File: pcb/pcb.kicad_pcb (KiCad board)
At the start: 2 copper layers, 190.5 x 85.7 mm, 98 parts, among them J1 OLED, SW1 RotaryEncoder_Switch, U1 Elite-C

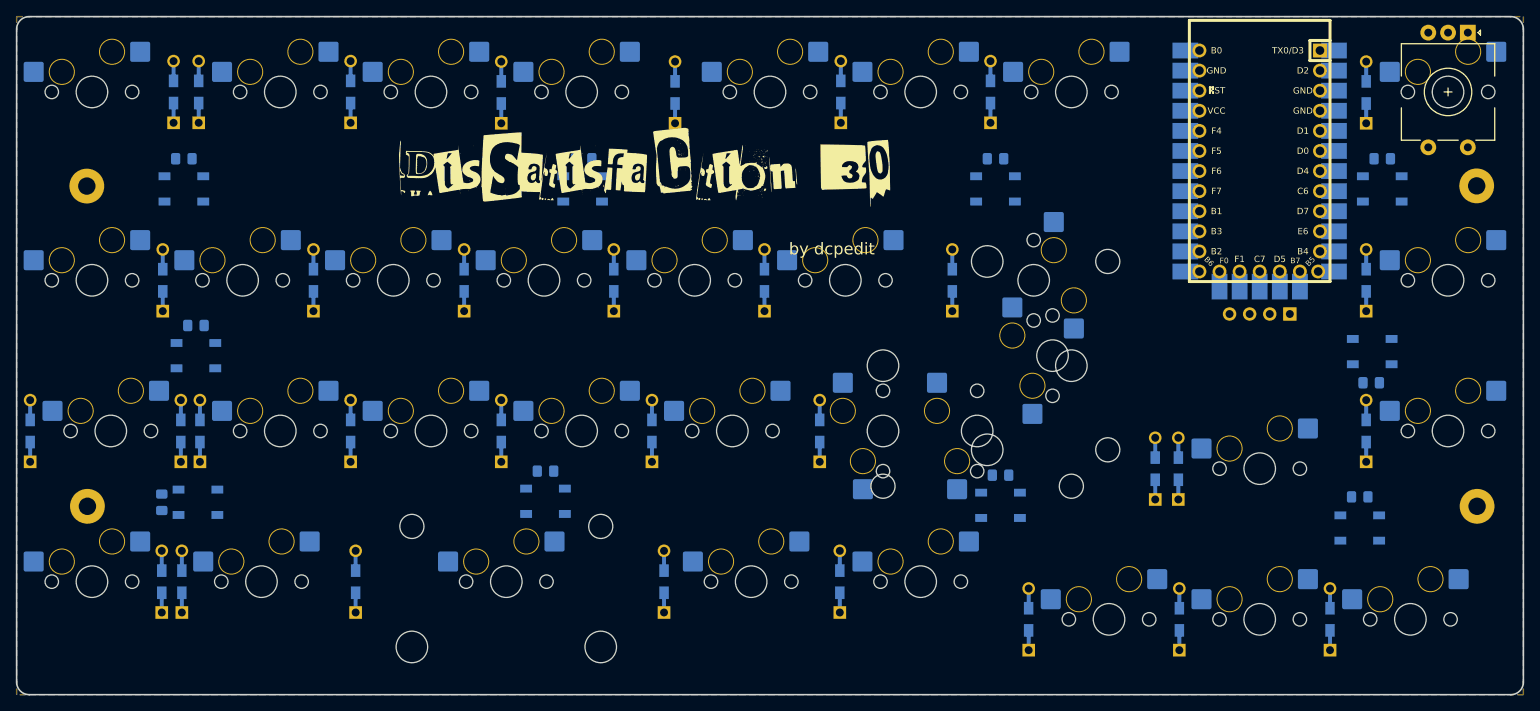
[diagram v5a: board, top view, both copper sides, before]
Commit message: Routed power and switch matrix. Pending connections to the MCU.
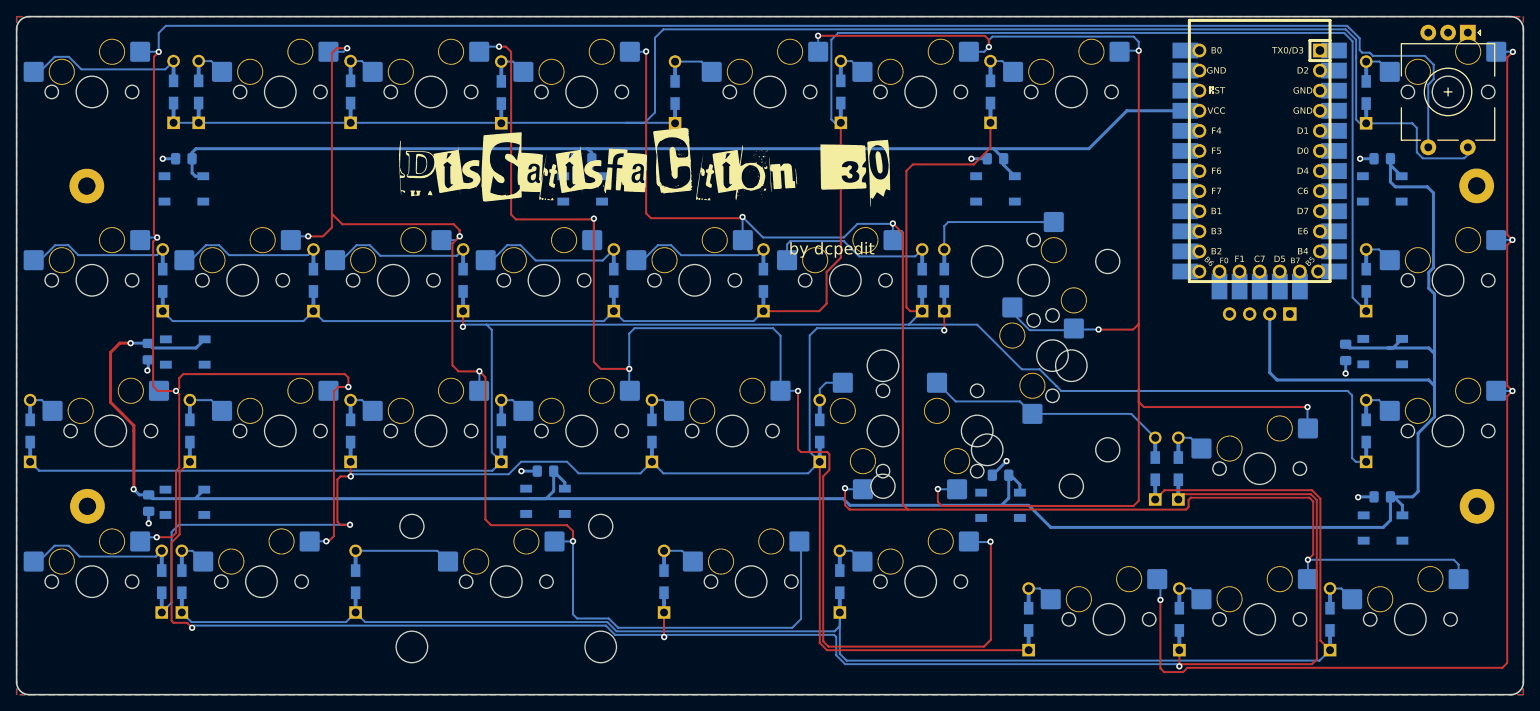
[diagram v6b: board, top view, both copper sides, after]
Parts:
- moved D14 40.5 mm to (70.7, 47.6)
- moved D16 19.9 mm to (128.8, 47.6)
- moved D10 18.9 mm to (108.7, 47.6)
- moved D9 18.9 mm to (89.8, 47.6)
- moved C10 6.87 mm to (30.9, 56.6), turned to -90 degrees
- moved C5 5.01 mm to (182.3, 56.7), turned to -90 degrees
- moved D39 2.95 mm to (187.0, 78.9)
- moved C6 2.84 mm to (186.9, 75.0)
- moved C9 1.65 mm to (31.0, 75.8)
- moved D42 1.65 mm to (35.6, 75.7)
- moved D43 1.42 mm to (35.6, 56.7)
- moved D38 1.32 mm to (187.0, 56.6)
- moved D30 1.27 mm to (36.2, 66.7)
- moved D23 1.02 mm to (131.6, 47.6)
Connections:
- D32 pad 1: Net-(D32-Pad1) -> ROW5
- D33 pad 1: Net-(D32-Pad1) -> ROW5
- MX22 pad 1: COL3 -> Net-(D22-Pad2)
- MX22 pad 2: Net-(D22-Pad2) -> COL3
- MX30 pad 1: COL4 -> Net-(D29-Pad2)
- MX30 pad 2: Net-(D29-Pad2) -> COL4
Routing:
- net +5V: track 0.00 -> 455.6 mm, vias 0 -> 2
- net COL0: track 0.00 -> 304.9 mm, vias 0 -> 6
- net ROW2: track 0.00 -> 243.6 mm, vias 0 -> 1
- net ROW1: track 0.00 -> 224.0 mm
- net ROW5: track 0.00 -> 213.8 mm, vias 0 -> 3
- net ROW4: track 0.00 -> 196.7 mm
- net ROW0: track 0.00 -> 196.3 mm
- net COL3: track 0.00 -> 194.2 mm, vias 0 -> 5
- net ROW3: track 0.00 -> 193.0 mm, vias 0 -> 3
- net COL4: track 0.00 -> 182.2 mm, vias 0 -> 6
- net COL2: track 0.00 -> 170.6 mm, vias 0 -> 5
- net COL1: track 0.00 -> 159.3 mm, vias 0 -> 5
- net COL5: track 0.00 -> 140.8 mm, vias 0 -> 4
- net Net-(D29-Pad2): track 0.00 -> 30.5 mm
- net Net-(D16-Pad2): track 0.00 -> 20.4 mm
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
